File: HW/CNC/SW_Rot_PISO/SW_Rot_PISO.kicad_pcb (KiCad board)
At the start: 2 copper layers, 101.6 x 76.2 mm, 18 parts, among them J1 1x13 2.54mm male 90deg, J2 1x8 2.54mm female 90deg, J3 1x13 2.54mm male 90deg, J4 1x13 2.54mm male 90deg, U1 74LS166, U2 74LS166

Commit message: Correction.
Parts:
- moved R1 2.54 mm to (205.7, 139.7)
- moved R10 2.54 mm to (180.3, 139.7)
- moved R11 2.54 mm to (210.8, 139.7)
- moved R12 2.54 mm to (208.3, 139.7)
- moved R2 2.54 mm to (203.2, 139.7)
- moved R3 2.54 mm to (200.7, 139.7)
- moved R4 2.54 mm to (198.1, 139.7)
- moved R5 2.54 mm to (193.0, 139.7)
- moved R6 2.54 mm to (190.5, 139.7)
- moved R7 2.54 mm to (188.0, 139.7)
- moved R8 2.54 mm to (185.4, 139.7)
- moved R9 2.54 mm to (182.9, 139.7)
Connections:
- net /LOAD renamed /N_LOAD
- U1 pad 6: VCC -> GND
- U2 pad 6: VCC -> GND
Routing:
- net VCC: track 134.6 -> 157.5 mm, vias 6 -> 8
- net GND: track 154.9 -> 172.7 mm, vias 10 -> 11

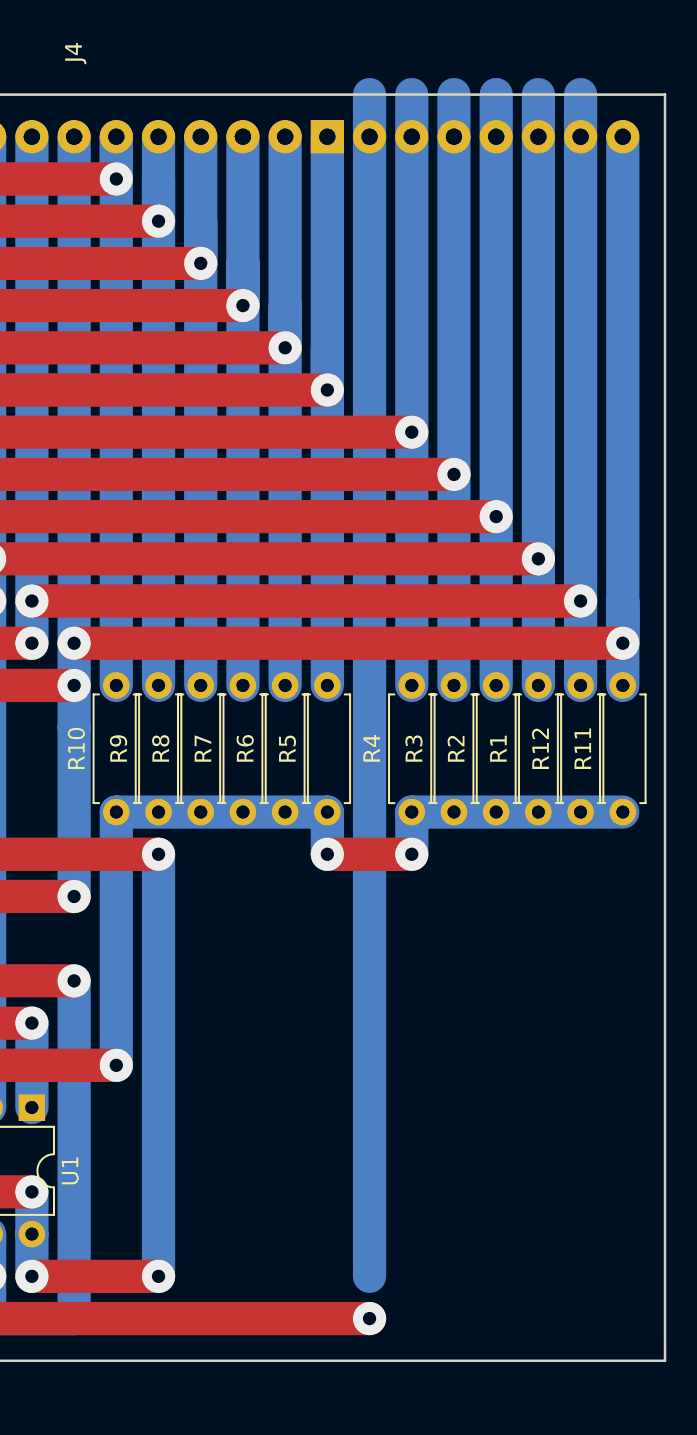
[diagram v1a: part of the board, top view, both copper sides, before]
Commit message: Corrections after soldering prototype.
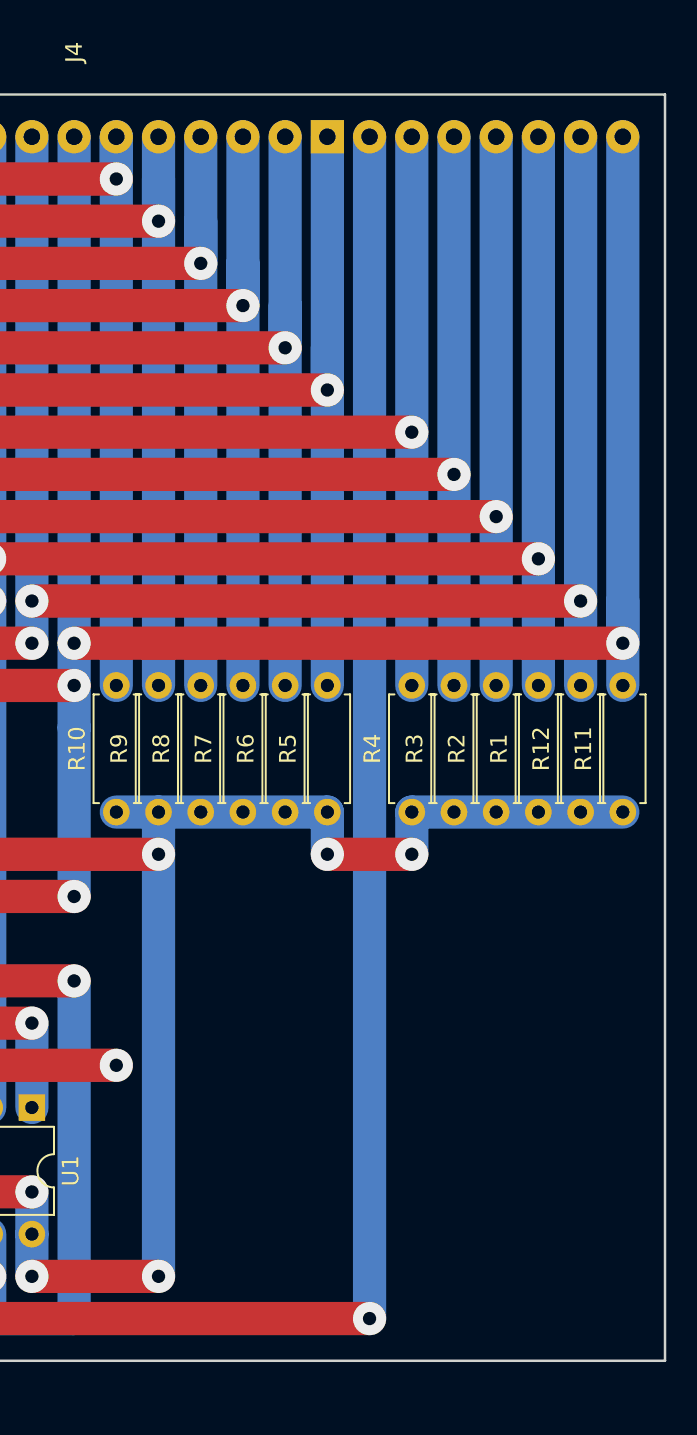
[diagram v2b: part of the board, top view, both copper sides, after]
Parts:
- R1, R10, R11, R12, R2, R3, R4, R5, R6, R7, R8, R9: value 1k -> 10k
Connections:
- net /R0 renamed /N_R0
- net /R1 renamed /N_R1
- net /R2 renamed /N_R2
- R1 pad 1: GND -> VCC
- R10 pad 1: GND -> VCC
- R11 pad 1: GND -> VCC
- R12 pad 1: GND -> VCC
- R2 pad 1: GND -> VCC
- R3 pad 1: GND -> VCC
- R4 pad 1: GND -> VCC
- R5 pad 1: GND -> VCC
- R6 pad 1: GND -> VCC
- R7 pad 1: GND -> VCC
- R8 pad 1: GND -> VCC
- R9 pad 1: GND -> VCC
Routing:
- net GND: track 172.7 -> 121.9 mm, vias 11 -> 9
- net VCC: track 157.5 -> 195.6 mm, vias 8 -> 10
- net /C10: track 182.9 -> 180.3 mm
- net /C08: track 188.0 -> 185.4 mm
- net /C07: track 200.7 -> 198.1 mm
- net /C11: track 180.3 -> 177.8 mm
- net /C09: track 185.4 -> 182.9 mm
